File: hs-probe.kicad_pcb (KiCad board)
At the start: 4 copper layers, 36.5 x 14 mm, 41 parts, among them J1 USB_C_Receptacle_USB2.0, U1 STM32F723IEKx, U2 DSC6003HI2A-012.0000T, U3 MIC5259-3.3YD5-TR, U4 NUF8401MNT4G, U5 STDC14, U6 SOICbite_SWD

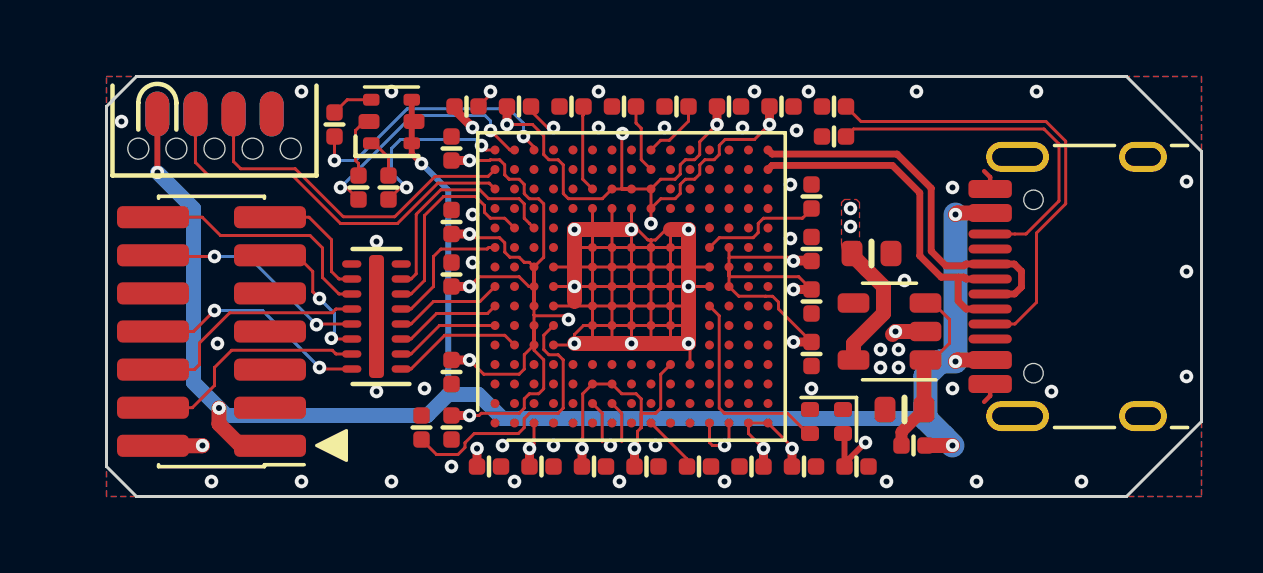
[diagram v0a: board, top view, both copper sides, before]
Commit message: Added JTAG on SPI2
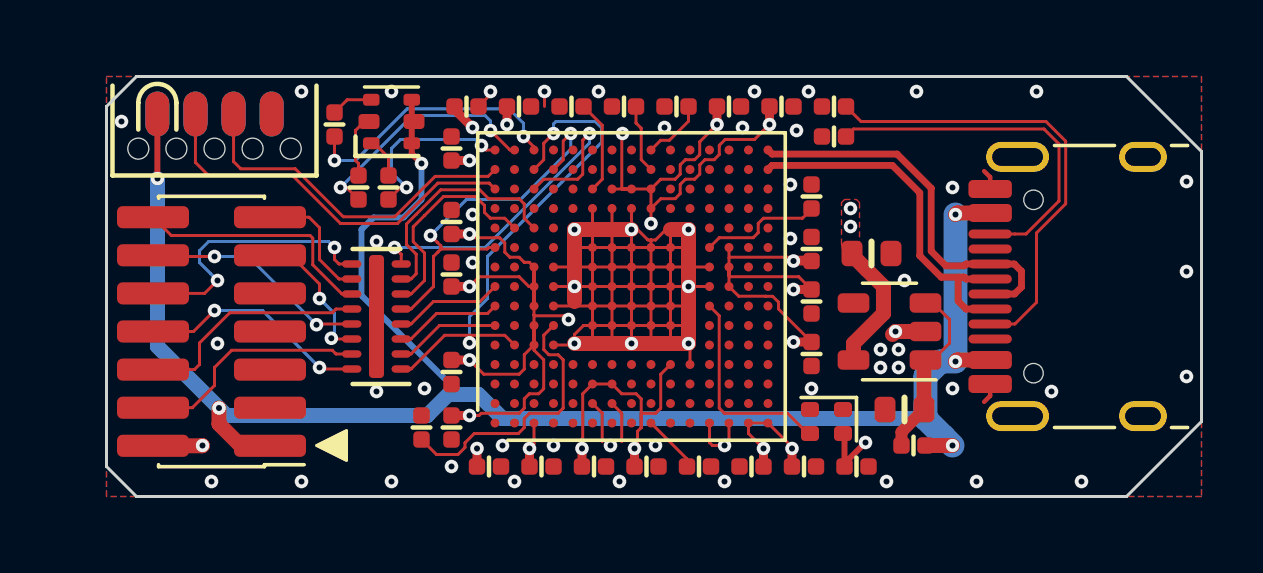
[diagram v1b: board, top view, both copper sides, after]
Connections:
- net /T_SWDCLK renamed /T_SWDCLK_JCLK
- net /T_SWDIO renamed /T_SWDIO_TMS
- net /T_SWO renamed /T_SWO_TDO
- U1 pad B5: /USART1_RX -> /SPI2_MISO
- U1 pad C13: Net-(U1-PadC13) -> /SPI2_MOSI
- U1 pad C14: Net-(U1-PadC14) -> /SPI2_MISO
- U1 pad D14: Net-(U1-PadD14) -> /SPI1_CLK
- U4 pad 1: /USART1_RX -> /SPI2_MISO
- U4 pad 8: Net-(U4-Pad8) -> /SPI2_MOSI
- U4 pad 9: Net-(U4-Pad9) -> /T_TDI
- U5 pad 10: Net-(U5-Pad10) -> /T_TDI
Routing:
- net /SPI2_MISO: track 0.00 -> 17.1 mm, vias 0 -> 2
- net /SPI2_MOSI: track 0.00 -> 12.2 mm, vias 0 -> 2
- net +3V3: track 94.5 -> 83.2 mm
- net /T_TDI: track 0.00 -> 9.32 mm, vias 0 -> 2
- net /SPI1_CLK: track 4.56 -> 13.0 mm, vias 0 -> 2
- net /USART1_RX: track 4.37 -> 0.00 mm
- net +5V: track 59.8 -> 62.1 mm
- net GND: track 68.5 -> 68.1 mm, vias 58 -> 57

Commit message: Minor updates
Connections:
- U6 pad 7: Net-(U6-Pad7) -> /NRST
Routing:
- net /NRST: track 1.95 -> 30.8 mm, vias 0 -> 1
- net GND: vias 57 -> 61

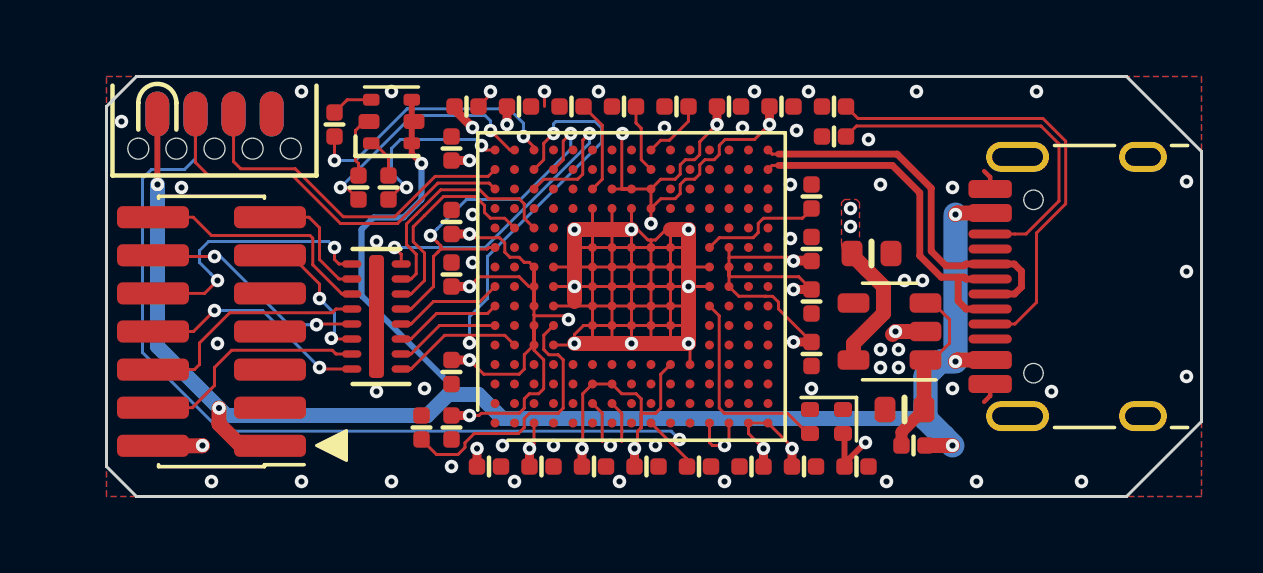
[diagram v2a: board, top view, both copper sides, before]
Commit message: Shorted SPI1 MISO/MOSI, rotated connector
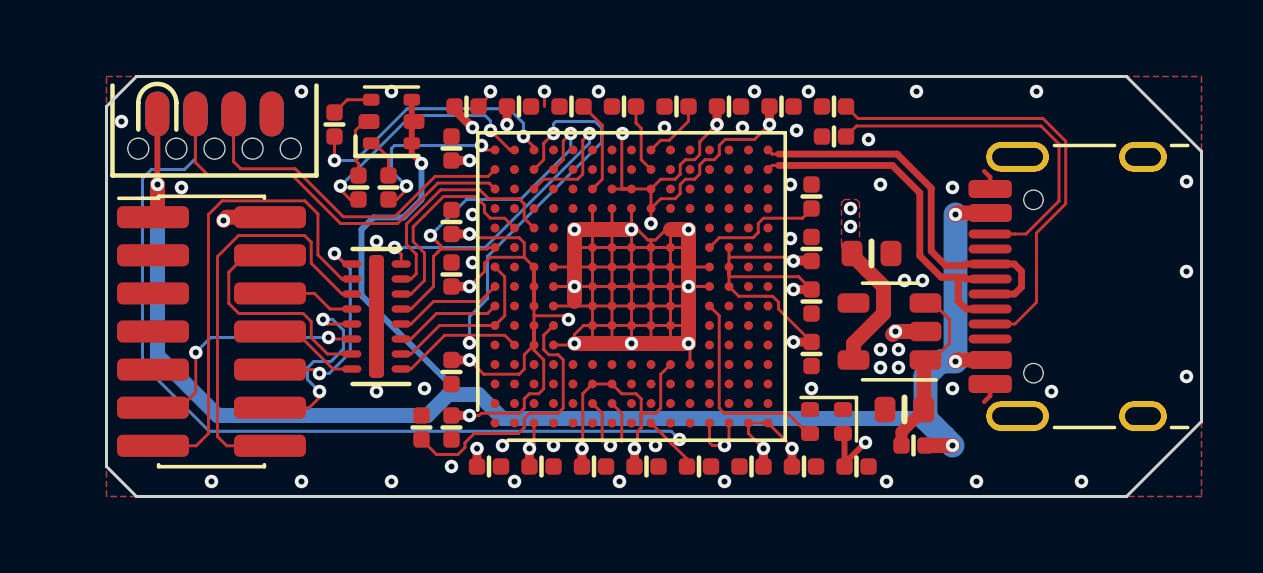
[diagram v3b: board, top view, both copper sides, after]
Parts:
- turned U5 to 0 degrees
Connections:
- U1 pad A6: /SPI1_MOSI -> /SPI1_MISO
- U4 pad 2: /SPI1_MOSI -> /SPI1_MISO
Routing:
- net /T_VCP_RX: track 4.20 -> 16.2 mm
- net /SPI1_MISO: track 0.00 -> 5.74 mm
- net /T_VCP_TX: track 8.20 -> 13.9 mm
- net /T_SWDCLK_JCLK: track 7.88 -> 2.94 mm
- net /T_SWO_TDO: track 7.72 -> 3.24 mm, vias 2 -> 0
- net /T_GNDDetect: track 4.80 -> 8.39 mm
- net /SPI1_MOSI: track 3.52 -> 0.00 mm
- net /T_TDI: track 9.32 -> 7.25 mm
- net +5V: track 62.1 -> 60.8 mm, vias 6 -> 5
- net /T_~RESET: track 7.59 -> 6.88 mm
- net GND: vias 61 -> 60

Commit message: Added ESD protection, fixed silkscreen
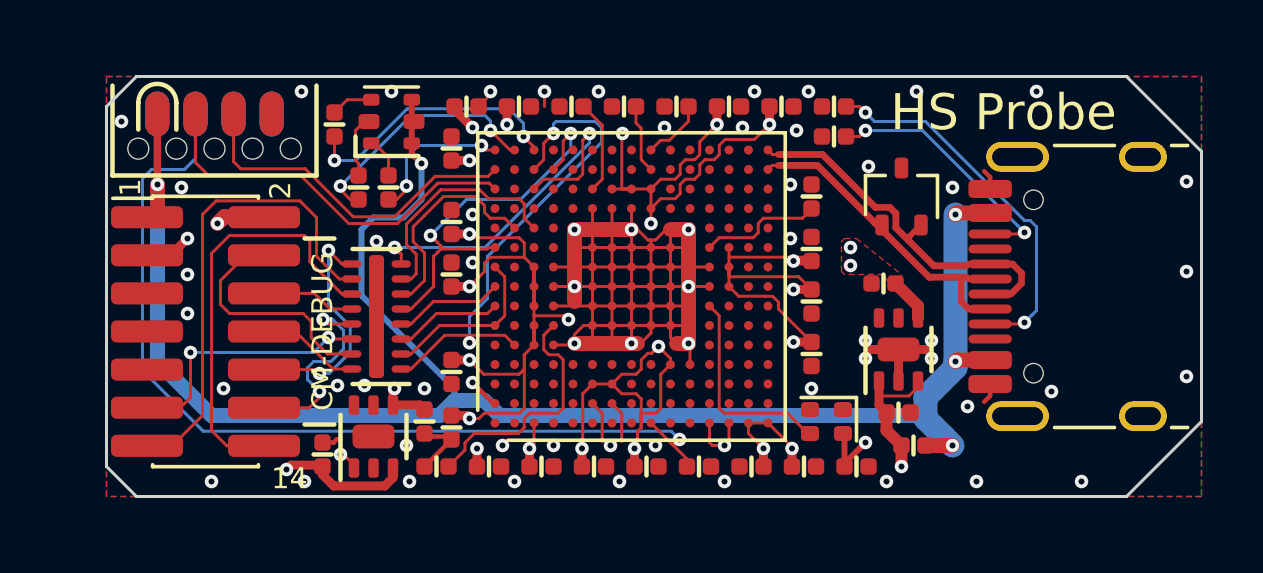
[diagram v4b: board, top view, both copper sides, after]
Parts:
- added C26: 2.2u, passive:C_0402, F.Cu at (175.9, 90.2)
- added C27: 2.2u, passive:C_0402, F.Cu at (160.1, 90.5)
- added D2: ESD7002WTT1G, sot:SOT-323, F.Cu at (176.0, 83.0)
- added U7: MIC5259, dfn:DFN-6-1EP_2x2mm_P0.65mm_EP1x1.6mm, F.Cu at (158.4, 91.0)
- C24, C25: value 4.7u -> 2.2u; footprint passive:C_0603 -> passive:C_0402
- U3: value MIC5259-3.3YD5-TR -> MIC5259; footprint sot:SOT-23-5 -> dfn:DFN-6-1EP_2x2mm_P0.65mm_EP1x1.6mm
- moved C24 19.5 mm to (156.7, 91.6), turned to 90 degrees
- moved R1 1.39 mm to (160.5, 92.0), turned to 180 degrees
- moved C25 1.08 mm to (175.4, 85.9), turned to 180 degrees
- moved U3 0.67 mm to (175.9, 88.1), turned to 90 degrees
- moved U5 0.20 mm to (152.8, 87.5)
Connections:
- U1 pad A2: Net-(U1-PadA2) -> /T_VCC_EN
- U3 pad 4: Net-(U3-Pad4) -> +3V3
- U3 pad 5: +3V3 -> (no net)
- U5 pad 3: Net-(U5-Pad3) -> /T_VCC
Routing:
- net Net-(C24-Pad1): track 6.03 -> 30.6 mm, vias 0 -> 2
- net /T_VCC: track 0.00 -> 12.9 mm, vias 0 -> 2
- net /T_VCC_EN: track 0.00 -> 7.13 mm, vias 0 -> 2
- net Net-(J1-PadB5): track 12.1 -> 8.61 mm, vias 0 -> 2
- net GND: track 68.1 -> 71.6 mm
- net Net-(J1-PadA5): track 15.4 -> 12.5 mm, vias 0 -> 2
- net /D_N: track 12.4 -> 11.3 mm
- net /BOOT0: track 9.18 -> 8.29 mm
- net /LED1: track 5.87 -> 4.99 mm
- net +3V3: track 82.9 -> 82.7 mm, vias 25 -> 26
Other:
- board text added: "1"
- board text added: "14"
- board text added: "2"
- board text added: "CM-DEBUG"
- board text added: "HS Probe"
- board text added: "HS Probe v1.0 By Emil Fresk @korken89"

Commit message: Updated LED for a more commonly available one
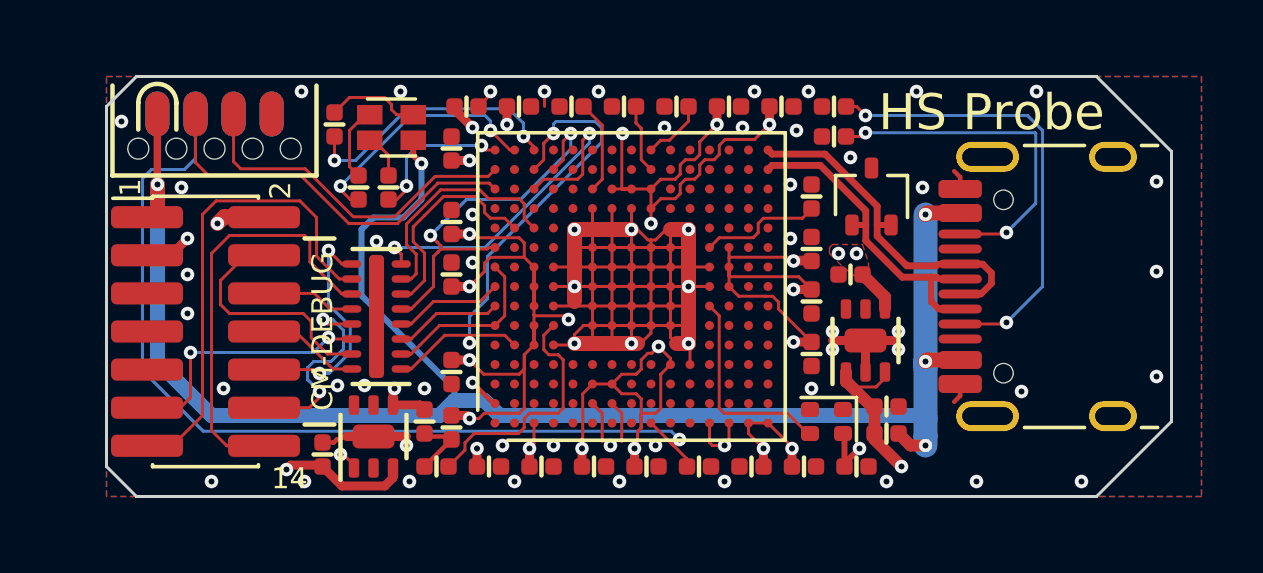
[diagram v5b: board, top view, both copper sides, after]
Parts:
- D1: value 19-337C/RSBHGHC-A88/4T -> LTST-C19HE1WT; footprint leds:0606 -> LED_SMD:LED_LiteOn_LTST-C19HE1WT
- moved C25 1.14 mm to (174.3, 85.6)
- moved U3 1.14 mm to (174.8, 87.8)
- moved D2 1.00 mm to (175.0, 83.0)
- moved J1 1.00 mm to (182.0, 86.0)
- moved FB1 0.98 mm to (175.5, 90.9)
- moved C26 0.45 mm to (175.5, 90.0)
- moved D1 0.20 mm to (159.0, 80.7), turned to 90 degrees
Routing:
- net Net-(J1-PadB5): track 8.61 -> 11.7 mm
- net Net-(J1-PadA5): track 12.5 -> 15.3 mm
- net GND: track 71.6 -> 73.8 mm, vias 60 -> 59
- net +5V: track 60.8 -> 59.0 mm
- net Net-(D1-Pad3): track 1.40 -> 3.17 mm
- net /D_P: track 12.7 -> 11.8 mm
- net Net-(C24-Pad1): track 30.6 -> 31.3 mm
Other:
- board size 36.5 x 14 mm -> 35.5 x 14 mm

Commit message: Fix errors
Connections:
- U1 pad A13: /P_SWDIO -> Net-(U1-PadA13)
- U1 pad A15: /LED1 -> /P_SWDIO
- U1 pad B14: Net-(U1-PadB14) -> /LED1
- U1 pad G1: Net-(U1-PadG1) -> /OSC
- U1 pad M7: /OSC -> Net-(U1-PadM7)
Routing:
- net +3V3: track 82.4 -> 80.2 mm
- net /LED1: track 4.99 -> 6.36 mm
- net /P_SWDIO: track 13.1 -> 14.4 mm

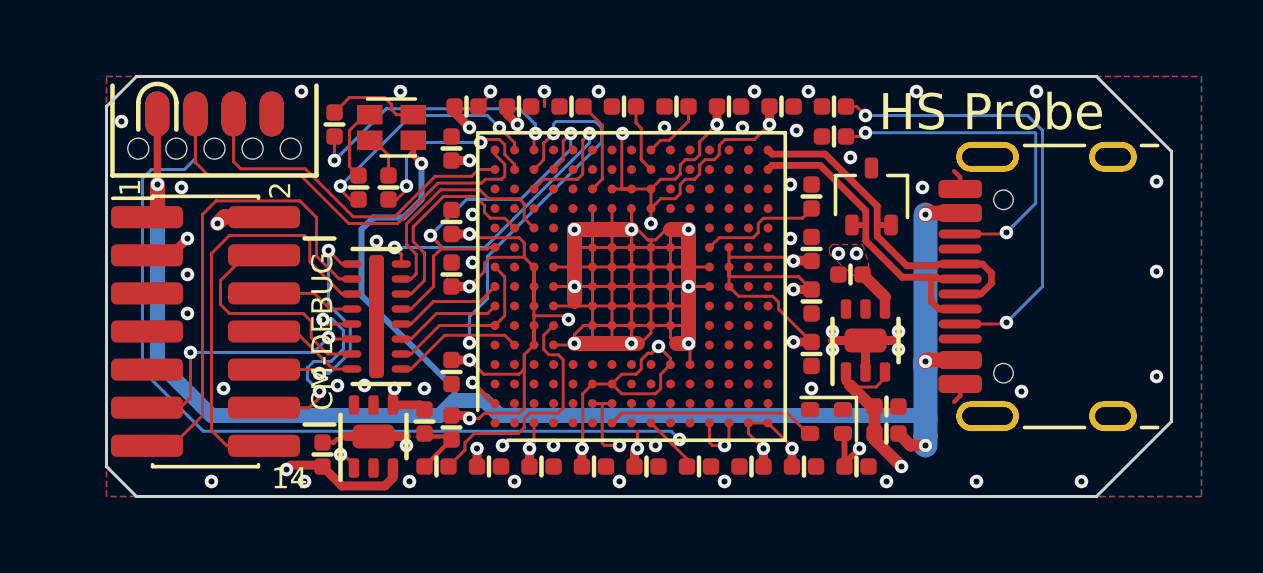
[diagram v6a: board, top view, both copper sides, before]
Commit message: Added USB Mux to start with FS and then switch to HS
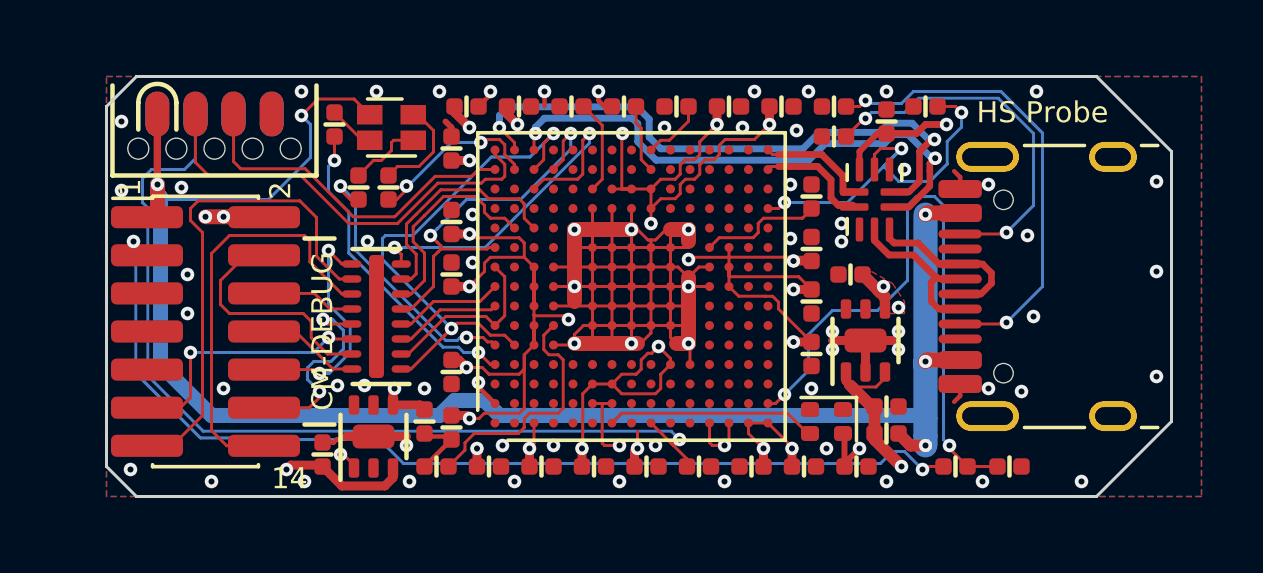
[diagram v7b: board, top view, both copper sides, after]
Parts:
- removed D2: ESD7002WTT1G, sot:SOT-323
- added C28: 0.1u, passive:C_0402, F.Cu at (175.5, 80.5)
- added R101: 5.1k, passive:R_0402, F.Cu at (179.6, 92.0)
- added R102: 5.1k, passive:R_0402, F.Cu at (177.8, 92.0)
- added R8: 5.1k, passive:R_0402, F.Cu at (176.8, 80.0)
- added U8: USB3740B-AI9, Package_DFN_QFN:UQFN-10_1.6x2.1mm_P0.5mm, F.Cu at (175.1, 83.1)
- turned D1 to 270 degrees
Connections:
- C27 pad 1: /T_VCC -> /T_VCC_PWR
- U1 pad A4: Net-(U1-PadA4) -> /LED3
- U1 pad A5: Net-(U1-PadA5) -> /LED2
- U1 pad B15: /LED2 -> /D_FS_P
- U1 pad C15: /LED3 -> /D_FS_N
- U1 pad R12: Net-(U1-PadR12) -> /USB_SEL
- U1 pad R14: /D_N -> /D_HS_N
- U1 pad R15: /D_P -> /D_HS_P
- U1 pad R2: Net-(U1-PadR2) -> /T_VCC_MEAS
- U5 pad 2: +3V3 -> /T_VCC_PWR
- U7 pad 4: /T_VCC -> /T_VCC_PWR
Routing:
- net /T_VCC: track 12.9 -> 34.0 mm
- net /T_VCC_MEAS: track 0.00 -> 21.0 mm, vias 0 -> 2
- net /D_FS_P: track 0.00 -> 20.1 mm, vias 0 -> 2
- net /D_FS_N: track 0.00 -> 18.3 mm, vias 0 -> 2
- net /T_VCC_PWR: track 0.00 -> 13.2 mm, vias 0 -> 3
- net /USB_SEL: track 0.00 -> 13.0 mm, vias 0 -> 3
- net /D_P: track 11.8 -> 5.72 mm
- net /D_N: track 11.1 -> 5.71 mm
- net /D_HS_N: track 0.00 -> 3.83 mm
- net /D_HS_P: track 0.00 -> 3.77 mm
- net Net-(D1-Pad1): track 1.51 -> 3.43 mm
- net +3V3: track 80.2 -> 78.3 mm, vias 26 -> 27
- net Net-(D1-Pad3): track 3.17 -> 1.56 mm
- net /LED3: track 9.30 -> 10.7 mm
- net +5V: track 59.0 -> 57.9 mm
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- added copper zone on In2.Cu, net +3V3
- removed copper zone on In1.Cu, net +3V3
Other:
- board text added: "HS Probe v1.1 By Emil Fresk @korken89"
- board text removed: "HS Probe v1.0 By Emil Fresk @korken89"

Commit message: Added Castellated Vias
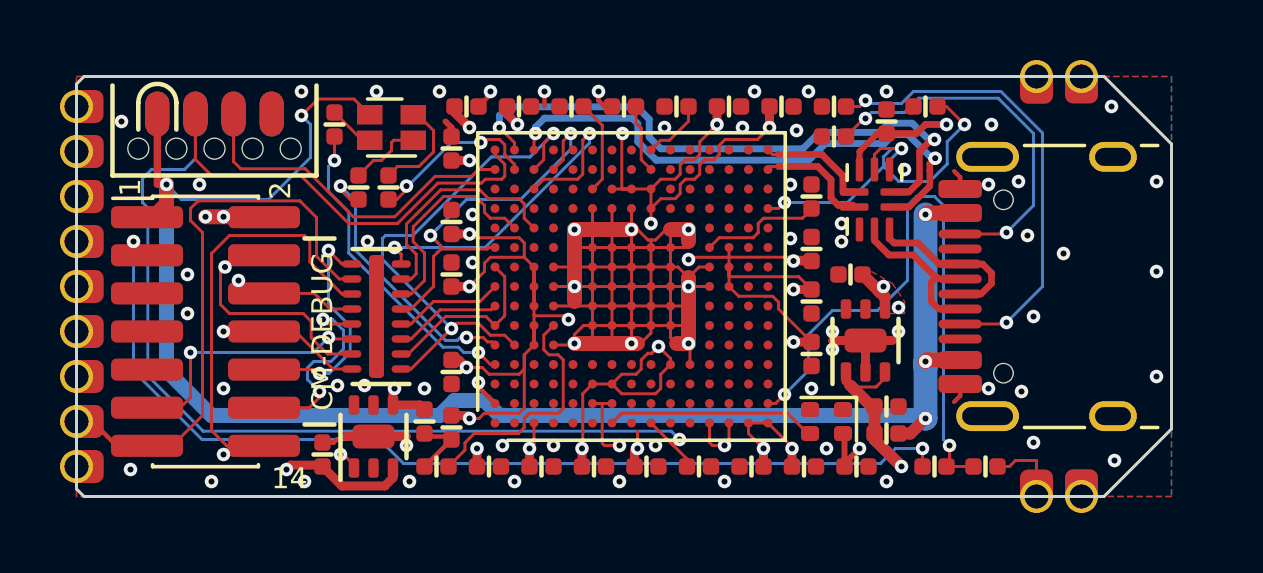
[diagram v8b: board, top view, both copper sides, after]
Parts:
- added J2: Conn_01x09_Female, connectors:1x9_1.5mm_castellated, F.Cu at (148.5, 80.0)
- added J3: Conn_01x02_Female, connectors:1x2_1.5mm_castellated, F.Cu at (180.5, 93.0)
- added J4: Conn_01x02_Female, connectors:1x2_1.5mm_castellated, F.Cu at (182.0, 79.0)
- moved R101 0.80 mm to (178.8, 92.0)
- moved R102 0.70 mm to (177.1, 92.0)
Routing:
- net /T_VCC_PWR: track 13.2 -> 42.3 mm
- net /T_VCC: track 34.0 -> 49.8 mm
- net /T_SWDCLK_JCLK: track 2.94 -> 12.3 mm, vias 0 -> 1
- net /T_TDI: track 7.68 -> 16.7 mm
- net /T_~RESET: track 6.88 -> 15.8 mm
- net /T_SWO_TDO: track 3.24 -> 11.8 mm, vias 0 -> 1
- net /T_SWDIO_TMS: track 8.17 -> 16.6 mm, vias 0 -> 1
- net /T_VCP_TX: track 14.2 -> 22.6 mm, vias 0 -> 1
- net +5V: track 57.9 -> 65.8 mm
- net /T_GNDDetect: track 8.49 -> 13.5 mm
- net GND: track 74.0 -> 77.8 mm, vias 68 -> 69
- net /T_VCP_RX: track 16.4 -> 19.5 mm
- net +3V3: track 78.3 -> 79.2 mm
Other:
- board size 35.5 x 14 mm -> 36.5 x 14 mm
- board text added: "3.3V"
- board text added: "5V"
- board text added: "CLK"
- board text added: "GDet"
- board text added: "GND"
- board text added: "IO"
- board text added: "RST"
- board text added: "RX"
- board text added: "SWO"
- board text added: "TDI"
- board text added: "TX"
- board text added: "VDet"
- board text removed: "HS Probe"
